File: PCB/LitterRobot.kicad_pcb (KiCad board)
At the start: 4 copper layers, 55 x 140 mm, 25 parts, among them J1 DF11C-4DP-2V(57), J2 DF11C-6DP-2V(57), J3 DF11C-8DP-2V(57), J4 DF11C-6DP-2V(57), J5 Conn_02x05_Odd_Even, SW1 PCB_Push_Button, SW2 PCB_Push_Button, SW3 PCB_Push_Button, SW4 PCB_Push_Button, SW5 PCB_Push_Button, SW6 PCB_Push_Button, U3 VEML6035

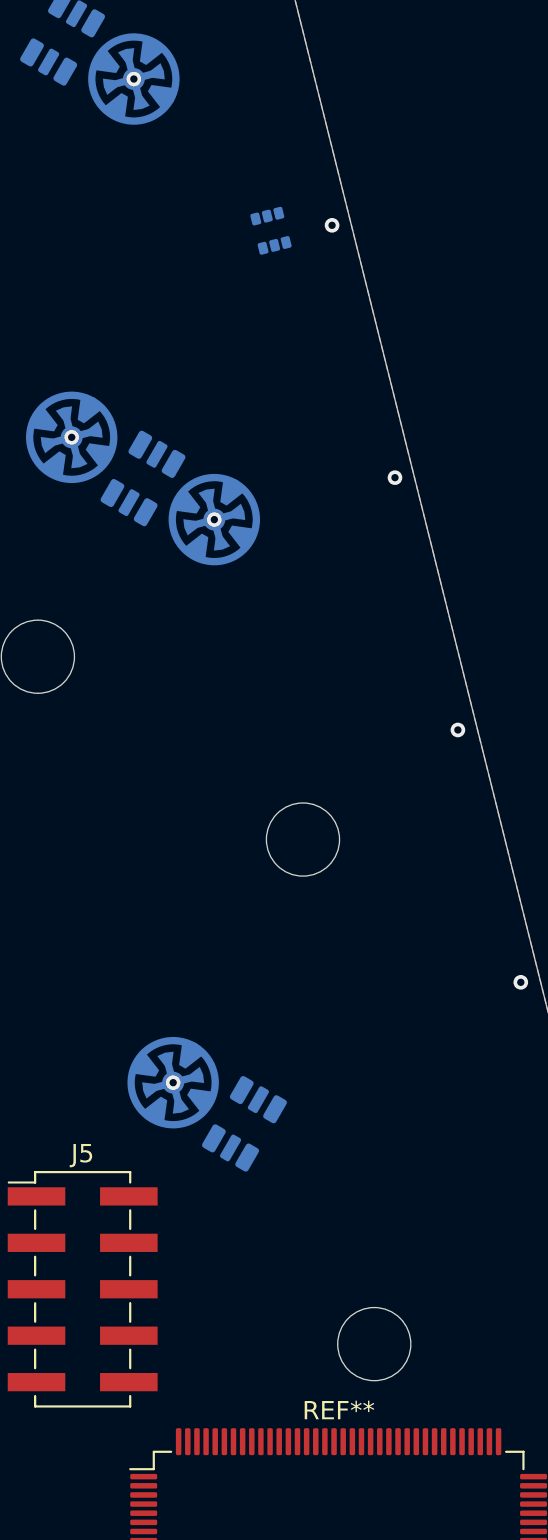
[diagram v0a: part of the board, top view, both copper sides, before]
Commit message: Add the FPGA symbol
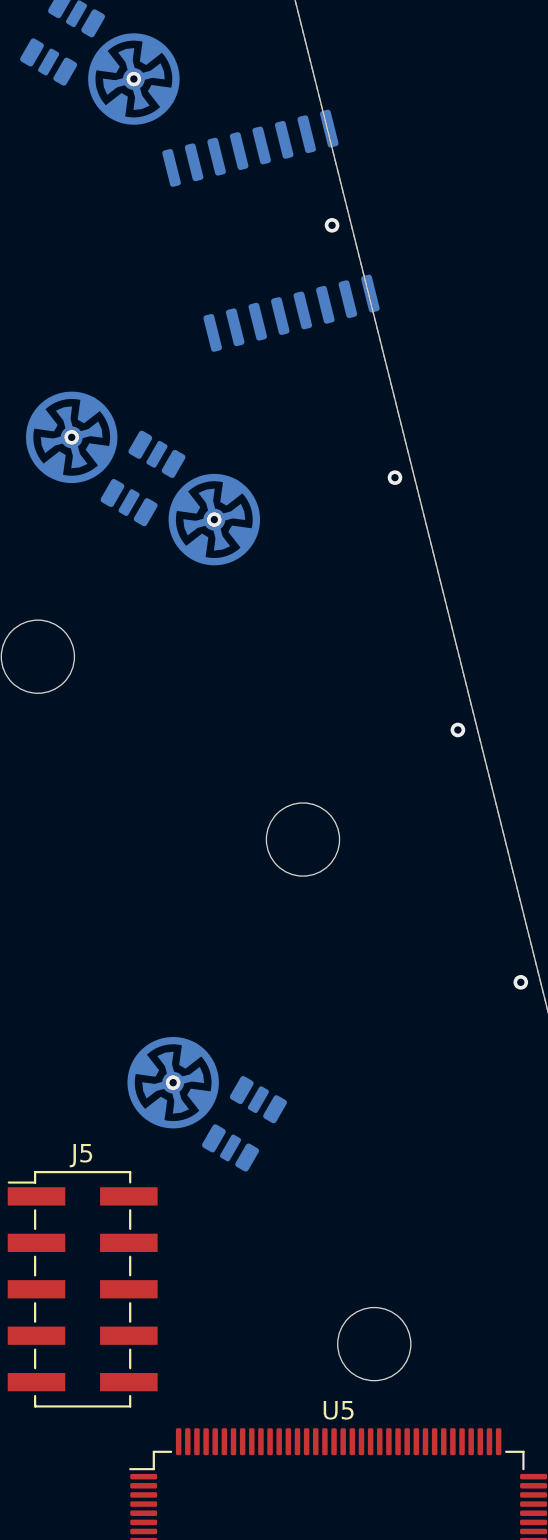
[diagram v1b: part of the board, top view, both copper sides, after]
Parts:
- removed REF**: Intel_EQFP-144-1EP_20x20mm_P0.5mm_EP6.7x6.7mm, LitterRobot:Intel_EQFP-144-1EP_20x20mm_P0.5mm_EP6.7x6.7mm
- added U5: 10CLxxxYE144, LitterRobot:Intel_EQFP-144-1EP_20x20mm_P0.5mm_EP6.7x6.7mm, F.Cu at (90.0, 127.0)
- J5: value Conn_02x05_Odd_Even -> TSM-105-01-S-DV
- U4: renamed from U3; value VEML6035 -> S25FL128SAGMFI000; footprint LitterRobot:Vishay_VEML6035 -> Package_SO:SOIC-16W_7.5x10.3mm_P1.27mm
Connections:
- J5 pad 10: (no net) -> GND
- J5 pad 2: (no net) -> GND
- J5 pad 4: (no net) -> +3V3
- U4 pad 1: GND -> (no net)
- U4 pad 2: /FPGA/Light_sensor_SDA -> +3V3
- U4 pad 3: /FPGA/Light_sensor_INT -> (no net)
- U4 pad 5: /FPGA/Light_sensor_SCL -> (no net)
- U4 pad 6: +3V3 -> (no net)

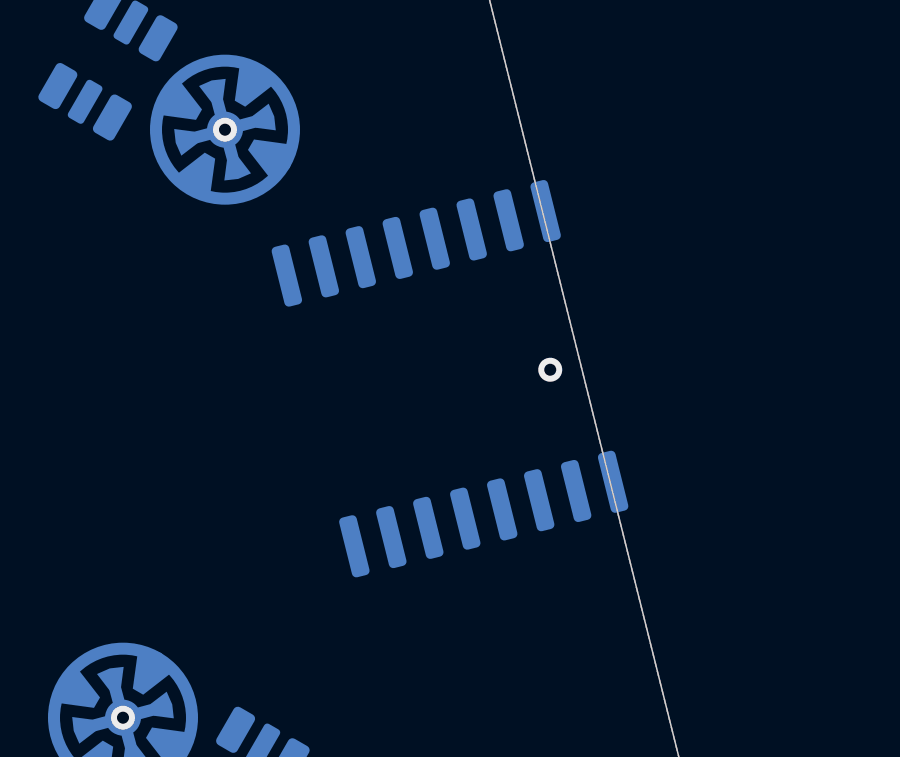
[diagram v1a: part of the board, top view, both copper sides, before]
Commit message: Connect the FPGA configuration signals
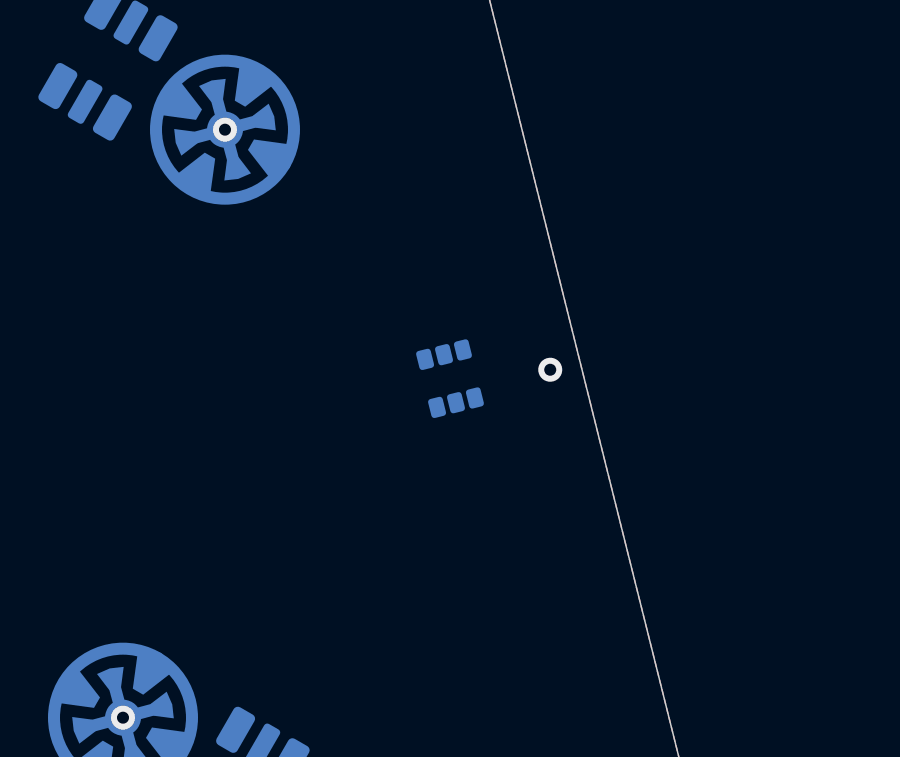
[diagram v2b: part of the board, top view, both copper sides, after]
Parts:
- removed U4: S25FL128SAGMFI000, Package_SO:SOIC-16W_7.5x10.3mm_P1.27mm
- added U3: VEML6035, LitterRobot:Vishay_VEML6035, B.Cu at (86.3, 50.1)
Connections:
- J5 pad 1: (no net) -> /FPGA/FPGA config/JTAG_TCK
- J5 pad 3: (no net) -> /FPGA/FPGA config/JTAG_TDO
- J5 pad 5: (no net) -> /FPGA/FPGA config/JTAG_TMS
- J5 pad 9: (no net) -> /FPGA/FPGA config/JTAG_TDI
- U5 pad 12: (no net) -> /FPGA/FPGA config/DCLK
- U5 pad 13: (no net) -> /FPGA/FPGA config/DATA0
- U5 pad 14: (no net) -> /FPGA/Power_good
- U5 pad 15: (no net) -> /FPGA/FPGA config/JTAG_TDI
- U5 pad 16: (no net) -> /FPGA/FPGA config/JTAG_TCK
- U5 pad 17: (no net) -> +3V3
- U5 pad 18: (no net) -> /FPGA/FPGA config/JTAG_TMS
- U5 pad 20: (no net) -> /FPGA/FPGA config/JTAG_TDO
- U5 pad 21: (no net) -> GND
- U5 pad 22: (no net) -> /FPGA/FPGA config/CLK_20MHz
- U5 pad 23: (no net) -> GND
- U5 pad 6: (no net) -> /FPGA/FPGA config/ASDO
- U5 pad 8: (no net) -> /FPGA/FPGA config/~CS
- U5 pad 9: (no net) -> Net-(R45-Pad2)
- U5 pad 90: (no net) -> GND
- U5 pad 91: (no net) -> GND
- U5 pad 92: (no net) -> Net-(R44-Pad2)
- U5 pad 93: (no net) -> +3V3
- U5 pad 94: (no net) -> Net-(JP2-Pad2)
- U5 pad 96: (no net) -> Net-(JP3-Pad2)
- U5 pad 97: (no net) -> Net-(JP4-Pad2)

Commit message: Cleaned up the schematics
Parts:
- U5: value 10CLxxxYE144 -> 10CL016YE144C8G
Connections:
- J4 pad 2: (no net) -> /Extension1
- J4 pad 3: (no net) -> /Extension2
- J4 pad 4: (no net) -> /Extension3
- J4 pad 5: (no net) -> /Extension4
- U5 pad 10: (no net) -> Net-(TP2-Pad1)
- U5 pad 11: (no net) -> Net-(TP3-Pad1)
- U5 pad 111: (no net) -> /FPGA/Light_sensor_SDA
- U5 pad 112: (no net) -> /FPGA/Light_sensor_SCL
- U5 pad 113: (no net) -> /FPGA/Light_sensor_INT
- U5 pad 117: (no net) -> +3V3
- U5 pad 120: (no net) -> /Control panel/Cycle_LED_R
- U5 pad 121: (no net) -> /Control panel/Cycle_LED_G
- U5 pad 122: (no net) -> +3V3
- U5 pad 125: (no net) -> /Control panel/Cycle_LED_B
- U5 pad 126: (no net) -> GND
- U5 pad 127: (no net) -> GND
- U5 pad 128: (no net) -> GND
- U5 pad 129: (no net) -> GND
- U5 pad 130: (no net) -> +3V3
- U5 pad 132: (no net) -> /Control panel/Power_LED_B
- U5 pad 133: (no net) -> /Control panel/Power_LED_G
- U5 pad 135: (no net) -> /FPGA/Power_LED_B
- U5 pad 139: (no net) -> +3V3
- U5 pad 145: (no net) -> GND
- U5 pad 24: (no net) -> GND
- U5 pad 25: (no net) -> GND
- U5 pad 26: (no net) -> +3V3
- U5 pad 28: (no net) -> /Power_button
- U5 pad 31: (no net) -> /Cycle_button
- U5 pad 32: (no net) -> /Empty_button
- U5 pad 33: (no net) -> /Reset_button
- U5 pad 39: (no net) -> /Control panel/Right_LED_R
- U5 pad 40: (no net) -> +3V3
- U5 pad 42: (no net) -> /Control panel/Right_LED_G
- U5 pad 43: (no net) -> /Control panel/Right_LED_B
- U5 pad 44: (no net) -> /FPGA/Motor_PWM_1
- U5 pad 46: (no net) -> /FPGA/Motor_PWM_2
- U5 pad 47: (no net) -> +3V3
- U5 pad 49: (no net) -> /Control panel/Center_LED_R
- U5 pad 50: (no net) -> /Control panel/Center_LED_G
- U5 pad 51: (no net) -> /Control panel/Center_LED_B
- U5 pad 52: (no net) -> GND
- U5 pad 53: (no net) -> GND
- U5 pad 54: (no net) -> GND
- U5 pad 55: (no net) -> GND
- U5 pad 56: (no net) -> +3V3
- U5 pad 59: (no net) -> /Extension1
- U5 pad 60: (no net) -> /Extension2
- U5 pad 62: (no net) -> +3V3
- U5 pad 65: (no net) -> /Extension3
- U5 pad 66: (no net) -> /Extension4
- U5 pad 69: (no net) -> /Control panel/Left_LED_R
- U5 pad 7: (no net) -> Net-(TP1-Pad1)
- U5 pad 71: (no net) -> /Control panel/Left_LED_G
- U5 pad 72: (no net) -> /Control panel/Left_LED_B
- U5 pad 76: (no net) -> /Control panel/Reset_LED_R
- U5 pad 77: (no net) -> /Control panel/Reset_LED_G
- U5 pad 80: (no net) -> /Control panel/Reset_LED_B
- U5 pad 81: (no net) -> +3V3
- U5 pad 85: (no net) -> /Control panel/Empty_LED_R
- U5 pad 86: (no net) -> /Control panel/Empty_LED_G
- U5 pad 87: (no net) -> /Control panel/Empty_LED_B
- U5 pad 88: (no net) -> GND
- U5 pad 89: (no net) -> GND
- U5 pad 94: Net-(JP2-Pad2) -> GND
- U5 pad 96: Net-(JP3-Pad2) -> +3V3
- U5 pad 97: Net-(JP4-Pad2) -> GND

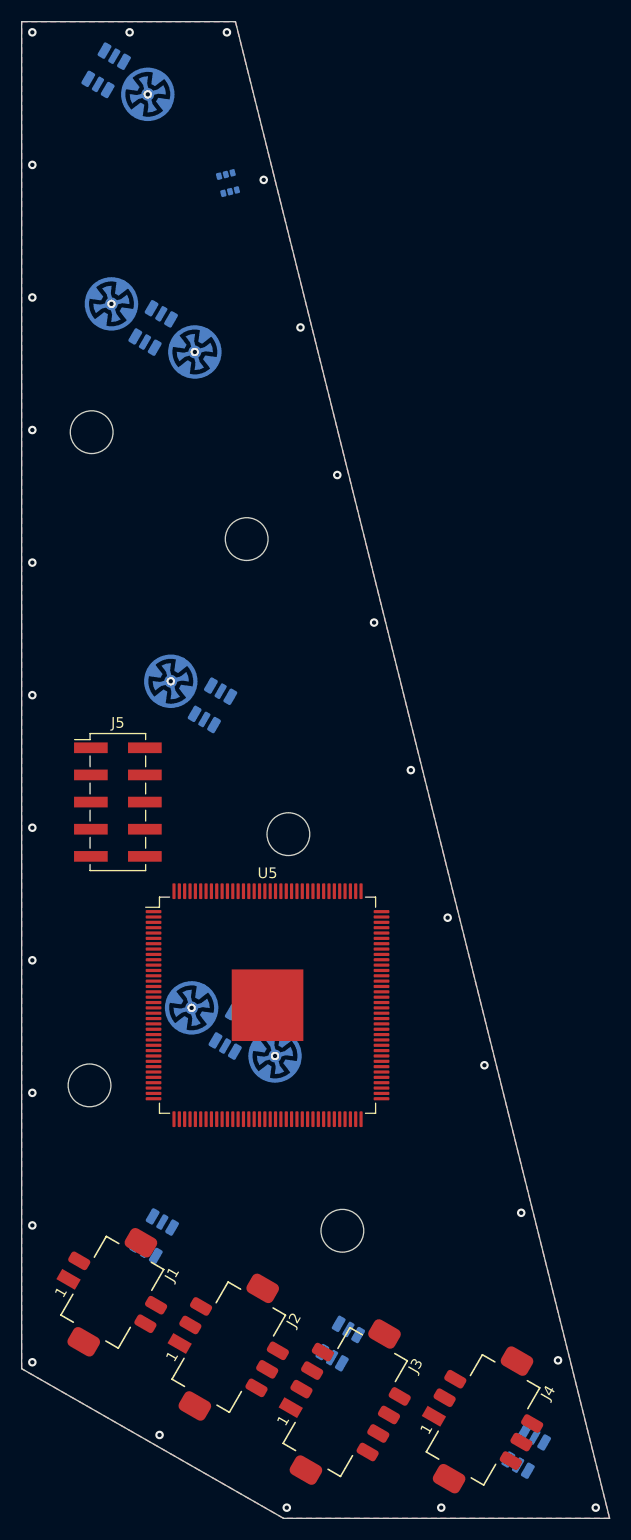
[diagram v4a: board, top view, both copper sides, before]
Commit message: Improve the push buttons
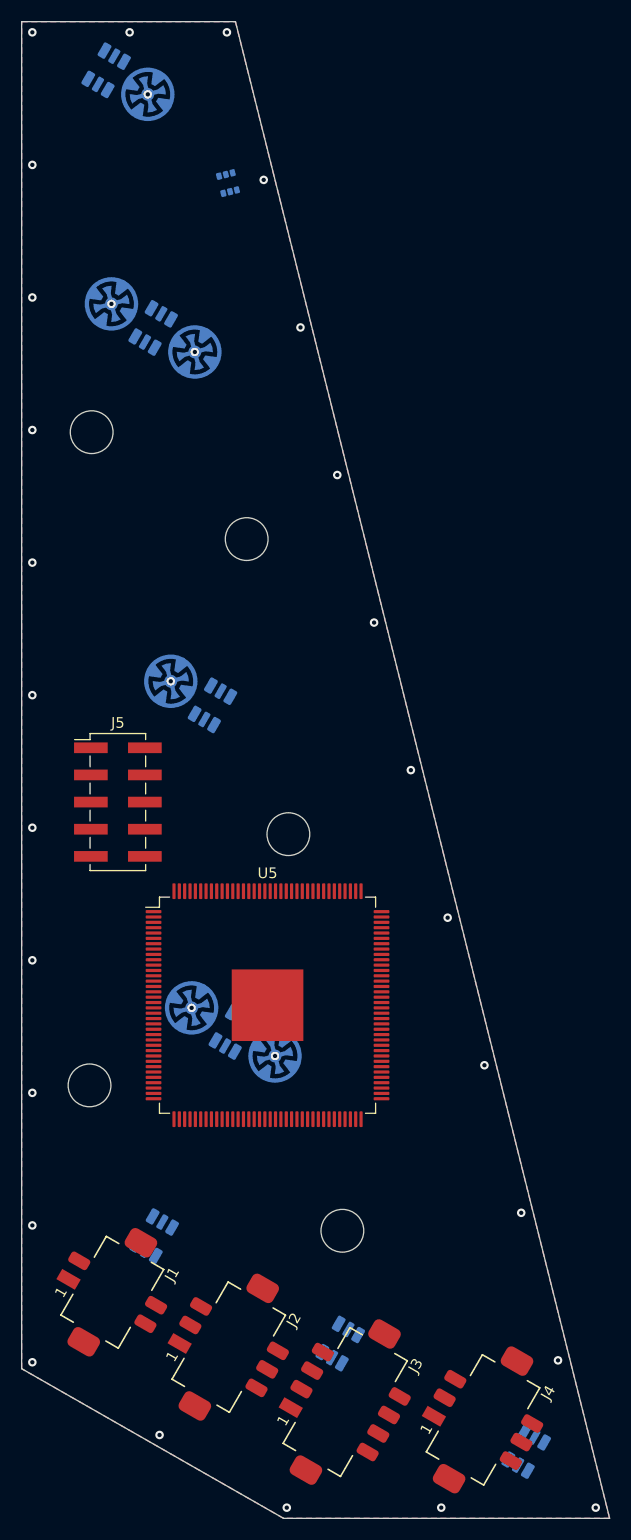
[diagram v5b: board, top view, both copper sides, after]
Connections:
- SW1 pad 1: +3V3 -> /Empty_button
- SW1 pad 2: /Empty_button -> GND
- SW2 pad 1: +3V3 -> /Power_button
- SW2 pad 2: /Power_button -> GND
- SW3 pad 1: +3V3 -> /Cycle_button
- SW3 pad 2: /Cycle_button -> GND
- SW4 pad 1: +3V3 -> /Cycle_button
- SW4 pad 2: /Cycle_button -> GND
- SW5 pad 1: +3V3 -> /Reset_button
- SW5 pad 2: /Reset_button -> GND
- SW6 pad 1: +3V3 -> /Reset_button
- SW6 pad 2: /Reset_button -> GND
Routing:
- net /Reset_button: vias 0 -> 2
- net /Power_button: vias 0 -> 1
- net /Empty_button: vias 0 -> 1
- net /Cycle_button: vias 0 -> 2
- net +3V3: vias 6 -> 0

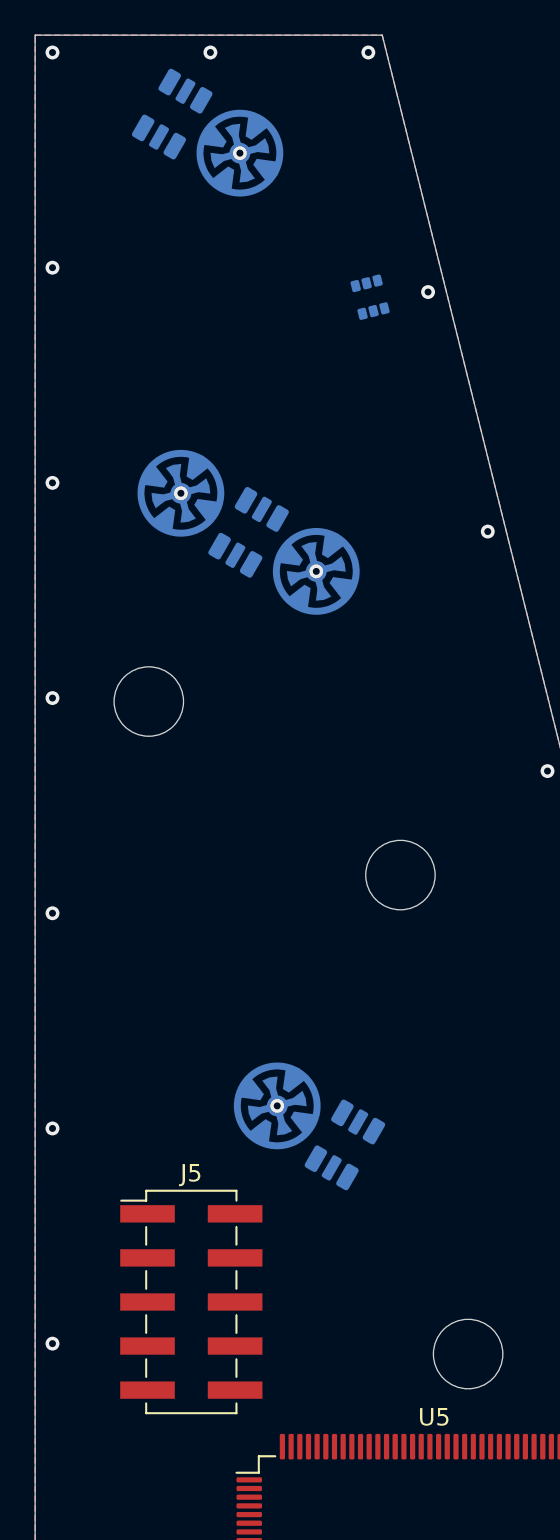
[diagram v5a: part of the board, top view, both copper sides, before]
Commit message: Add support for the weight sensor
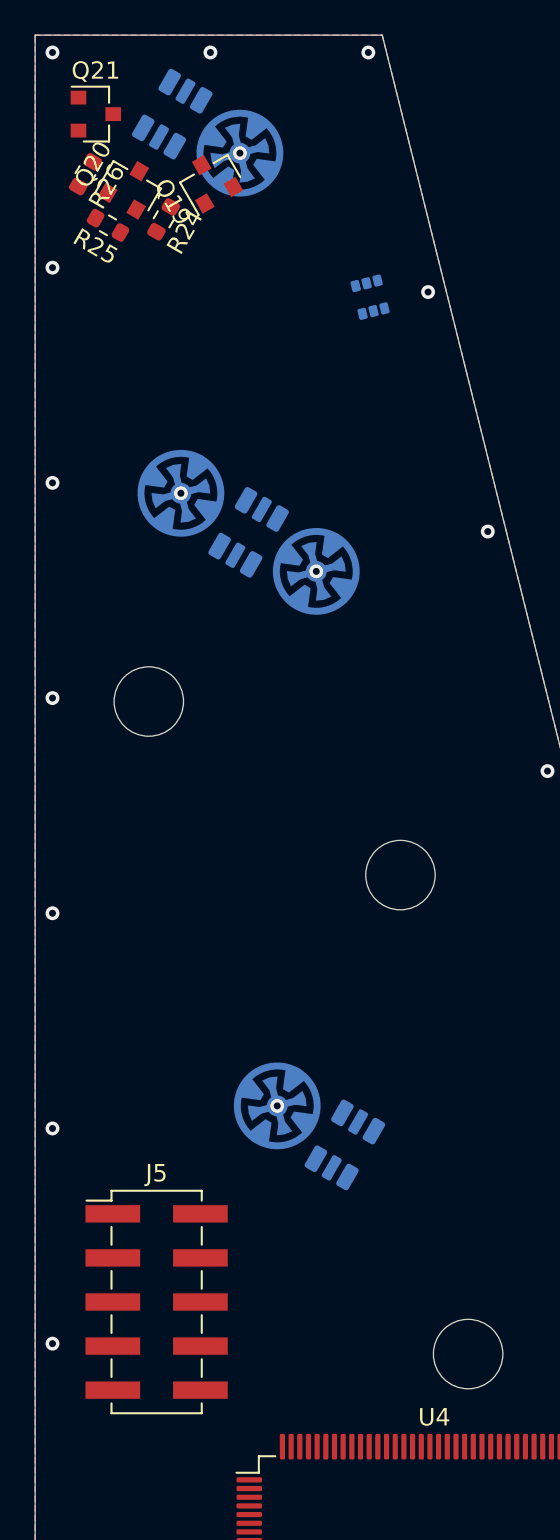
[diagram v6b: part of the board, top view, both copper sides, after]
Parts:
- added Q19: BC817, Package_TO_SOT_SMD:SOT-23, F.Cu at (77.1, 43.4)
- added Q20: BC817, Package_TO_SOT_SMD:SOT-23, F.Cu at (72.5, 43.7)
- added Q21: BC817, Package_TO_SOT_SMD:SOT-23, F.Cu at (70.5, 39.5)
- added R24: 178R, Resistor_SMD:R_0603_1608Metric, F.Cu at (74.4, 45.6)
- added R25: 221R, Resistor_SMD:R_0603_1608Metric, F.Cu at (71.2, 46.0)
- added R26: 221R, Resistor_SMD:R_0603_1608Metric, F.Cu at (69.9, 43.0)
- moved J5 2.00 mm to (74.0, 108.0)
- renumbered U5 to U4
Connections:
- net Net-(F1-Pad2) renamed /Power_P
- J1 pad 2: (no net) -> /DFI_1
- J1 pad 3: (no net) -> /DFI_2
- J2 pad 6: (no net) -> /Battery_P
- J3 pad 5: (no net) -> /Weight_sensor_P
- J3 pad 6: GND -> /Weight_sensor_N
- J4 pad 2: /Extension1 -> /Extension_1
- J4 pad 3: /Extension2 -> /Extension_2
- J4 pad 4: /Extension3 -> /Extension_3
- J4 pad 5: /Extension4 -> /Extension_4
- U4 pad 141: (no net) -> /Extension_1
- U4 pad 142: (no net) -> /Extension_2
- U4 pad 143: (no net) -> /Extension_3
- U4 pad 144: (no net) -> /Extension_4
- U4 pad 59: /Extension1 -> /DFI_1
- U4 pad 60: /Extension2 -> /DFI_2
- U4 pad 65: /Extension3 -> (no net)
- U4 pad 66: /Extension4 -> /FPGA/Weight_ref
- U4 pad 67: (no net) -> /Weight_sensor_P
- U4 pad 68: (no net) -> /Weight_sensor_N
